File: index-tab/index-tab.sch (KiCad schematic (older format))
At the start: 18 parts, among them J1 USB_C_Receptacle_USB2.0, SW1 SW_Push, U1 ATmega32U2-AU, Y1 Crystal_GND24

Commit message: Updated somevalues, and fixed the pin layout
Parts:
- C4, C5: value C -> 22p
- F1: value Polyfuse -> 500mA
- R1, R2: value R -> 5.1K
- Y1: value Crystal_GND24 -> 16MHz
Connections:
- net labels added: COL10, COL11, COL12, COL6, COL7, COL8, COL9
- net labels removed: ROW10, ROW11, ROW12, ROW6, ROW7, ROW8, ROW9
- wire segments 110 -> 111
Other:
- moved on the sheet: R2
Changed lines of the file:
@@
 P 3700 2450
 F 0 "C4" V 3448 2450 50  0000 C CNN
-F 1 "C" V 3539 2450 50  0000 C CNN
+F 1 "22p" V 3539 2450 50  0000 C CNN
 F 2 "" H 3738 2300 50  0001 C CNN
 F 3 "~" H 3700 2450 50  0001 C CNN
@@
 P 3700 2850
 F 0 "C5" V 3448 2850 50  0000 C CNN
-F 1 "C" V 3539 2850 50  0000 C CNN
+F 1 "22p" V 3539 2850 50  0000 C CNN
 F 2 "" H 3738 2700 50  0001 C CNN
 F 3 "~" H 3700 2850 50  0001 C CNN
@@
 P 4100 2650
 F 0 "Y1" V 4146 2406 50  0000 R CNN
-F 1 "Crystal_GND24" V 4055 2406 50  0000 R CNN
+F 1 "16MHz" V 4055 2406 50  0000 R CNN
 F 2 "" H 4100 2650 50  0001 C CNN
 F 3 "~" H 4100 2650 50  0001 C CNN
@@
 L power:GND #PWR06
 U 1 1 5E49637F
-P 2600 2450
-F 0 "#PWR06" H 2600 2200 50  0001 C CNN
-F 1 "GND" H 2605 2277 50  0000 C CNN
-F 2 "" H 2600 2450 50  0001 C CNN
-F 3 "" H 2600 2450 50  0001 C CNN
-	1    2600 2450
+P 2650 2450
+F 0 "#PWR06" H 2650 2200 50  0001 C CNN
+F 1 "GND" H 2655 2277 50  0000 C CNN
+F 2 "" H 2650 2450 50  0001 C CNN
+F 3 "" H 2650 2450 50  0001 C CNN
+	1    2650 2450
 	-1   0    0    1
 $EndComp
@@
 L Device:R R2
 U 1 1 5E496DB2
-P 2700 2700
-F 0 "R2" H 2630 2654 50  0000 R CNN
-F 1 "R" H 2630 2745 50  0000 R CNN
-F 2 "" V 2630 2700 50  0001 C CNN
-F 3 "~" H 2700 2700 50  0001 C CNN
-	1    2700 2700
+P 2800 2700
+F 0 "R2" H 2730 2654 50  0000 R CNN
+F 1 "5.1K" H 2730 2745 50  0000 R CNN
+F 2 "" V 2730 2700 50  0001 C CNN
+F 3 "~" H 2800 2700 50  0001 C CNN
+	1    2800 2700
 	-1   0    0    1
 $EndComp
@@
 P 2450 2700
 F 0 "R1" H 2380 2654 50  0000 R CNN
-F 1 "R" H 2380 2745 50  0000 R CNN
+F 1 "5.1K" H 2380 2745 50  0000 R CNN
 F 2 "" V 2380 2700 50  0001 C CNN
 F 3 "~" H 2450 2700 50  0001 C CNN
@@
 $EndComp
 Wire Wire Line
-	2700 2550 2600 2550
-Wire Wire Line
-	2600 2550 2600 2450
-Wire Wire Line
-	2450 2550 2600 2550
-Connection ~ 2600 2550
-Wire Wire Line
 	2100 3100 2450 3100
 Wire Wire Line
 	2450 3100 2450 2850
 Wire Wire Line
-	2100 3200 2700 3200
-Wire Wire Line
-	2700 3200 2700 2850
+	2800 3200 2800 2850
 $Comp
 L power:+5V #PWR05
@@
 P 2250 2050
 F 0 "F1" H 2338 2096 50  0000 L CNN
-F 1 "Polyfuse" H 2338 2005 50  0000 L CNN
+F 1 "500mA" H 2338 2005 50  0000 L CNN
 F 2 "" H 2300 1850 50  0001 L CNN
 F 3 "~" H 2250 2050 50  0001 C CNN
@@
 	2850 3450 3000 3450
 Text GLabel 6700 3850 2    50   Input ~ 0
+COL6
+Text GLabel 6700 3950 2    50   Input ~ 0
+COL7
+Text GLabel 6700 4050 2    50   Input ~ 0
+COL8
+Text GLabel 6700 4150 2    50   Input ~ 0
+COL9
+Text GLabel 6700 4250 2    50   Input ~ 0
+COL10
+Text GLabel 6700 4350 2    50   Input ~ 0
+COL11
+Wire Wire Line
+	6500 3850 6700 3850
+Wire Wire Line
+	6500 3950 6700 3950
+Wire Wire Line
+	6500 4050 6700 4050
+Wire Wire Line
+	6500 4150 6700 4150
+Wire Wire Line
+	6500 4250 6700 4250
+Wire Wire Line
+	6500 4350 6700 4350
+Text GLabel 6700 2950 2    50   Input ~ 0
 COL0
-Text GLabel 6700 3950 2    50   Input ~ 0
+Text GLabel 6700 3050 2    50   Input ~ 0
 COL1
-Text GLabel 6700 4050 2    50   Input ~ 0
+Text GLabel 6700 3250 2    50   Input ~ 0
 COL2
-Text GLabel 6700 4150 2    50   Input ~ 0
+Text GLabel 6700 3350 2    50   Input ~ 0
 COL3
-Text GLabel 6700 4250 2    50   Input ~ 0
+Text GLabel 6700 3450 2    50   Input ~ 0
 COL4
-Text GLabel 6700 4350 2    50   Input ~ 0
+Text GLabel 6700 3550 2    50   Input ~ 0
 COL5
-Wire Wire Line
-	6500 3850 6700 3850
-Wire Wire Line
-	6500 3950 6700 3950
-Wire Wire Line
-	6500 4050 6700 4050
-Wire Wire Line
-	6500 4150 6700 4150
-Wire Wire Line
-	6500 4250 6700 4250
-Wire Wire Line
-	6500 4350 6700 4350
-Text GLabel 6700 2350 2    50   Input ~ 0
-ROW0
-Text GLabel 6700 2450 2    50   Input ~ 0
-ROW1
-Text GLabel 6700 2550 2    50   Input ~ 0
-ROW2
-Text GLabel 6700 2650 2    50   Input ~ 0
-ROW3
-Text GLabel 6700 2750 2    50   Input ~ 0
-ROW4
-Text GLabel 6700 2850 2    50   Input ~ 0
-ROW5
-Text GLabel 6700 2950 2    50   Input ~ 0
-ROW6
-Text GLabel 6700 3050 2    50   Input ~ 0
-ROW7
-Text GLabel 6700 3250 2    50   Input ~ 0
-ROW8
-Text GLabel 6700 3350 2    50   Input ~ 0
-ROW9
-Text GLabel 6700 3450 2    50   Input ~ 0
-ROW10
-Text GLabel 6700 3550 2    50   Input ~ 0
-ROW11
 Text GLabel 6700 4450 2    50   Input ~ 0
-ROW12
+COL12
 Wire Wire Line
 	6500 2350 6700 2350
@@
 F1 "matrix.sch" 50
 $EndSheet
+Wire Wire Line
+	2100 3200 2800 3200
+Wire Wire Line
+	2650 2450 2800 2450
+Wire Wire Line
+	2800 2450 2800 2550
+Wire Wire Line
+	2450 2550 2450 2450
+Wire Wire Line
+	2450 2450 2650 2450
+Connection ~ 2650 2450
+Text GLabel 6700 2850 2    50   Input ~ 0
+ROW5
+Text GLabel 6700 2750 2    50   Input ~ 0
+ROW4
+Text GLabel 6700 2650 2    50   Input ~ 0
+ROW3
+Text GLabel 6700 2550 2    50   Input ~ 0
+ROW2
+Text GLabel 6700 2450 2    50   Input ~ 0
+ROW1
+Text GLabel 6700 2350 2    50   Input ~ 0
+ROW0
 $EndSCHEMATC

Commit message: Change to u4, added files for backlight and rgb
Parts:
- removed U1: ATmega32U2-AU, Package_QFP:TQFP-32_7x7mm_P0.8mm, symbol MCU_Microchip_ATmega:ATmega32U2-AU
- added LS1: Speaker, symbol Device:Speaker
- added R7: 1K, symbol Device:R
- added U1: ATmega32U4-MU, Package_DFN_QFN:QFN-44-1EP_7x7mm_P0.5mm_EP5.2x5.2mm, symbol MCU_Microchip_ATmega:ATmega32U4-MU
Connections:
- net labels added: BACKLIGHT, RGB
- wire segments 111 -> 120
- no-connect marks 2 -> 7
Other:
- moved on the sheet: C4, C5, C6, R5, R6, SW1, Y1

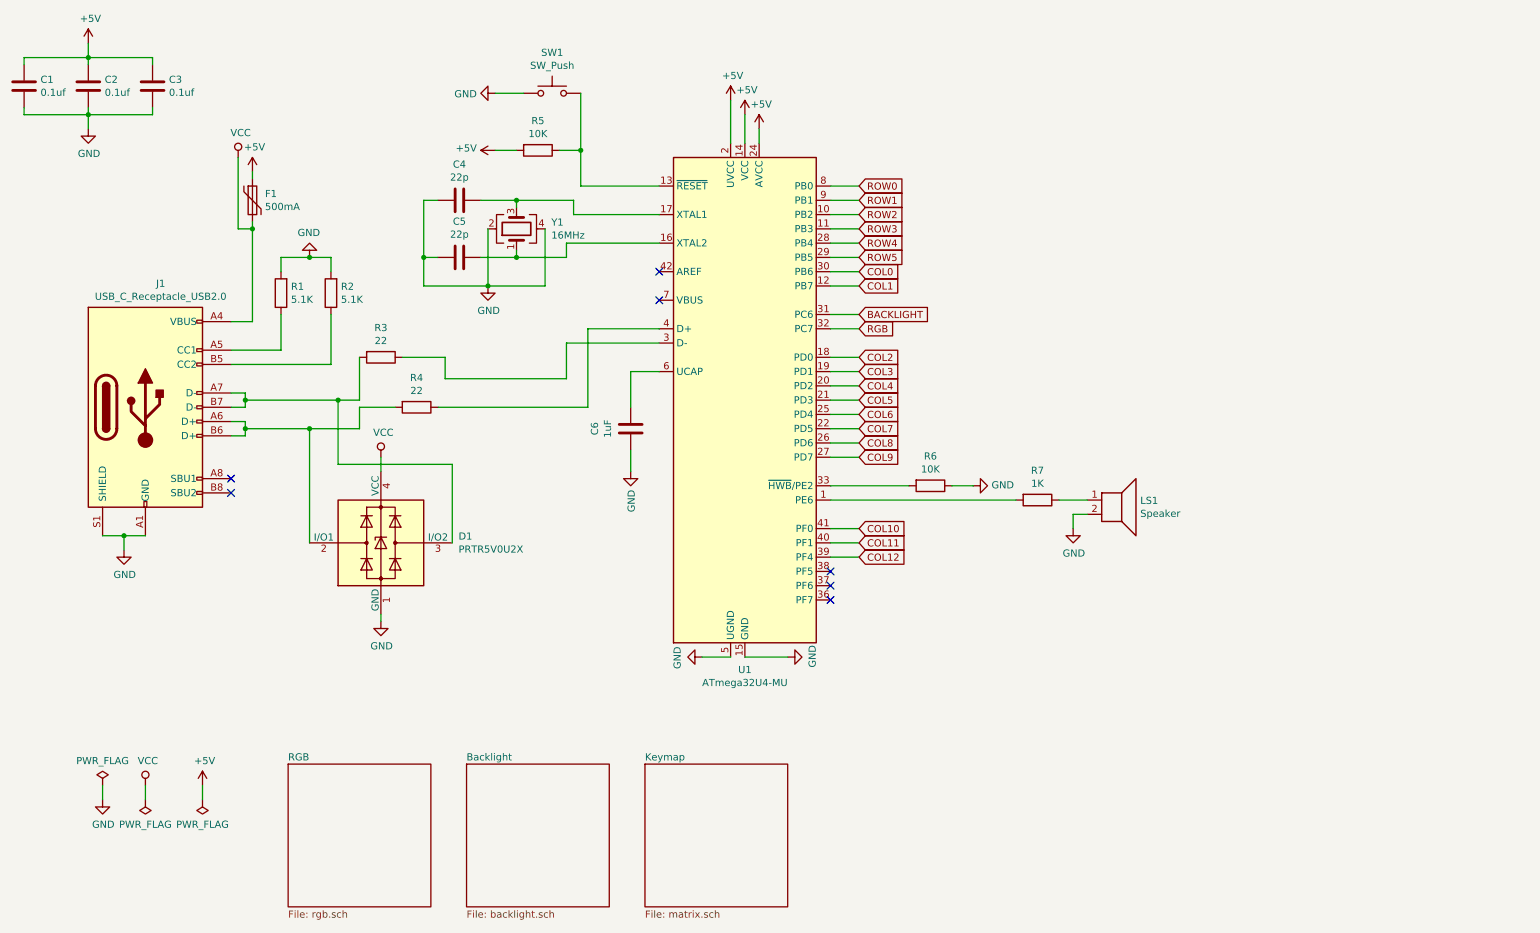
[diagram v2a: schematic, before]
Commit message: changed some labels, and hopefully done with the atmega32u4 changes
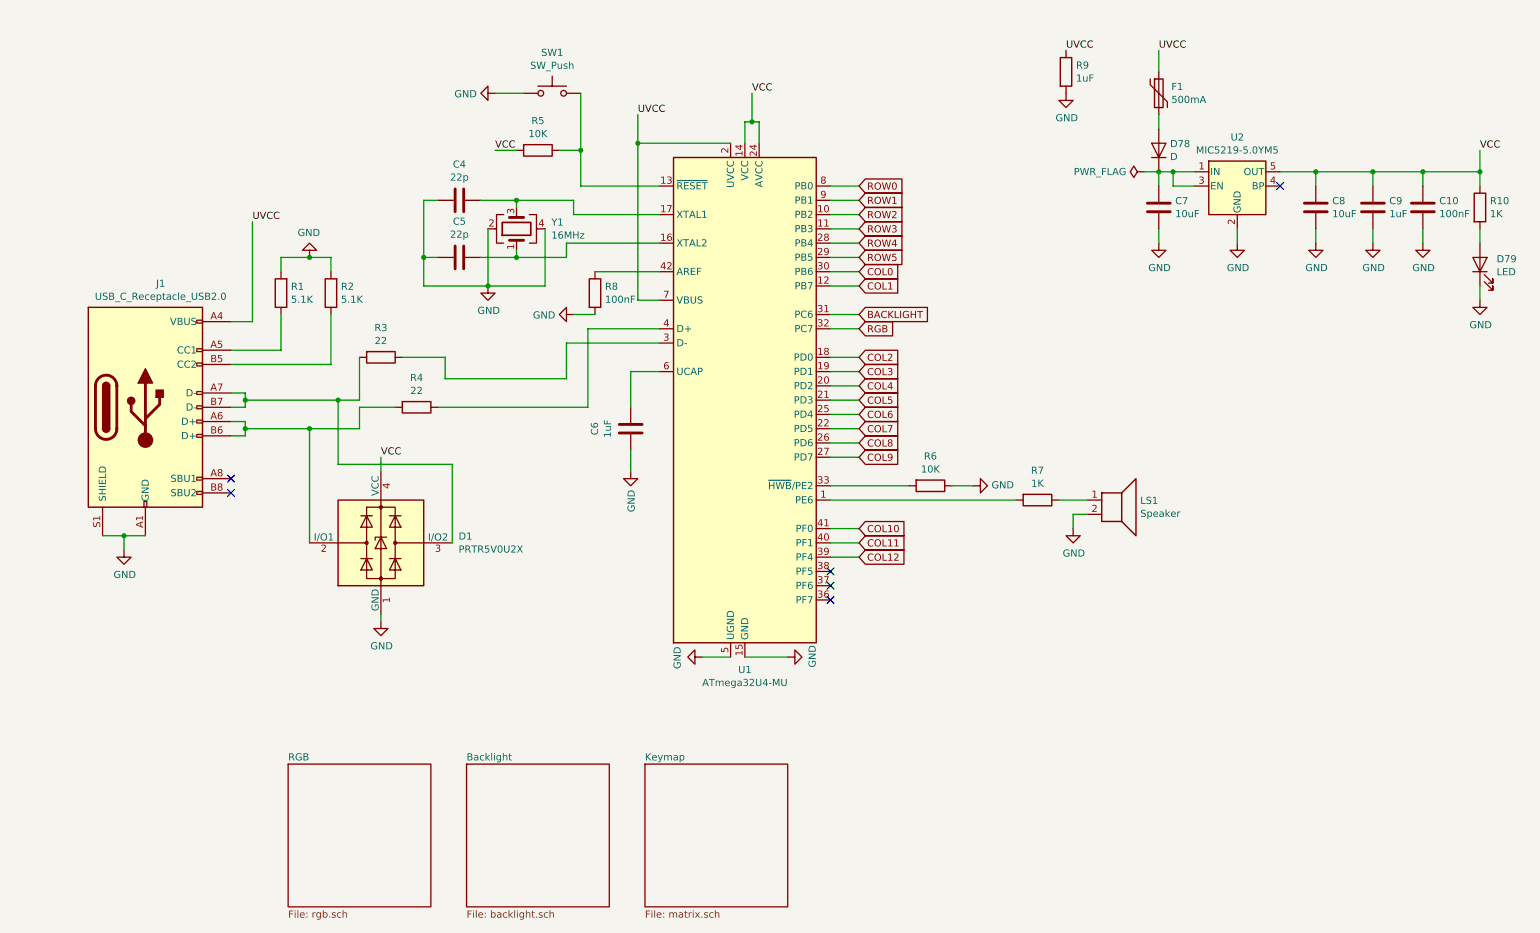
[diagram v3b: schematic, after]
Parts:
- removed C1, C2, C3: 0.1uf, symbol Device:C
- added C10: 100nF, symbol Device:C
- added C7, C8: 10uF, symbol Device:C
- added C9: 1uF, symbol Device:C
- added D78: D, symbol Device:D
- added D79: LED, symbol Device:LED
- added R10: 1K, symbol Device:R
- added R8: 100nF, symbol Device:R
- added R9: 1uF, symbol Device:R
- added U2: MIC5219-5.0YM5, Package_TO_SOT_SMD:SOT-23-5, symbol Regulator_Linear:MIC5219-5.0YM5
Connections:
- net GND: now also C10.2, C7.2, C8.2, C9.2, D79.1 (K), R8.2, R9.2, U2.2 (GND)
- net VCC: now also R5.2, U1.14 (VCC), U1.24 (AVCC), U1.34 (VCC), U1.44 (AVCC), C10.1, C8.1, C9.1, R10.1, U2.5 (OUT); no longer F1.2, J1.A4 (VBUS), J1.A9 (VBUS), J1.B4 (VBUS), J1.B9 (VBUS)
- net at U1.42 (AREF): now also R8.1
- net UVCC: now reaches U1.7 (VBUS)
- net UVCC: now also F1.1, J1.A4 (VBUS), J1.A9 (VBUS), J1.B4 (VBUS), J1.B9 (VBUS), U1.2 (UVCC), R9.1
- removed net +5V: F1.1, R5.2, U1.14 (VCC), U1.2 (UVCC), U1.24 (AVCC), U1.34 (VCC), U1.44 (AVCC)
- new net: D79.2 (A), R10.2
- new net: C7.1, D78.1 (K), U2.1 (IN), U2.3 (EN)
- new net: D78.2 (A), F1.2
- no-connect marks 7 -> 6
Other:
- moved on the sheet: F1

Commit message: Added footprints to all components, and done some formatting
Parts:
- removed R8: 100nF, symbol Device:R
- removed R9: 1uF, symbol Device:R
- added C1: 100nF, Capacitor_SMD:C_0603_1608Metric_Pad1.05x0.95mm_HandSolder, symbol Device:C
- added C2: 1uF, Capacitor_SMD:C_0603_1608Metric_Pad1.05x0.95mm_HandSolder, symbol Device:C
- C10, C4, C5, C6, C7, C8, C9: footprint (none) -> Capacitor_SMD:C_0603_1608Metric_Pad1.05x0.95mm_HandSolder
- D78: footprint (none) -> Diode_SMD:D_SOD-123
- D79: footprint (none) -> LED_THT:LED_D3.0mm_FlatTop
- F1: footprint (none) -> Fuse:Fuse_0805_2012Metric_Pad1.15x1.40mm_HandSolder
- J1: footprint (none) -> Connector_USB:USB_C_Receptacle_HRO_TYPE-C-31-M-12
- LS1: footprint (none) -> Buzzer_Beeper:Buzzer_12x9.5RM7.6
- R1, R10, R2, R3, R4, R5, R6, R7: footprint (none) -> Resistor_SMD:R_0201_0603Metric
- SW1: footprint (none) -> Button_Switch_SMD:SW_SPST_CK_RS282G05A3
- Y1: footprint (none) -> Crystal:Crystal_SMD_3225-4Pin_3.2x2.5mm_HandSoldering
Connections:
- net GND: now also C5.1, C1.1, C2.2; no longer C5.2
- net UVCC: now also C2.1
- net XTAL1: now reaches U1.17 (XTAL1), Y1.3
- net XTAL1: now also C5.2; no longer C4.1
- net XTAL2: now reaches U1.16 (XTAL2), Y1.1
- net XTAL2: now also C4.1; no longer C5.1
- net at U1.42 (AREF): now also C1.2
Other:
- moved on the sheet: C4, C5, D1, R1, R2, R3, R4, Y1

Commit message: Working PCB, plus images
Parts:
- removed LS1: Speaker, Buzzer_Beeper:Buzzer_12x9.5RM7.6, symbol Device:Speaker
- removed R7: 1K, Resistor_SMD:R_0201_0603Metric, symbol Device:R
- C1: renamed from C4; footprint Capacitor_SMD:C_0603_1608Metric_Pad1.05x0.95mm_HandSolder -> Capacitor_SMD:C_1206_3216Metric_Pad1.42x1.75mm_HandSolder
- C2: renamed from C5; footprint Capacitor_SMD:C_0603_1608Metric_Pad1.05x0.95mm_HandSolder -> Capacitor_SMD:C_1206_3216Metric_Pad1.42x1.75mm_HandSolder
- C3: renamed from C1; footprint Capacitor_SMD:C_0603_1608Metric_Pad1.05x0.95mm_HandSolder -> Capacitor_SMD:C_1206_3216Metric_Pad1.42x1.75mm_HandSolder
- C4: renamed from C6; footprint Capacitor_SMD:C_0603_1608Metric_Pad1.05x0.95mm_HandSolder -> Capacitor_SMD:C_1206_3216Metric_Pad1.42x1.75mm_HandSolder
- C5: renamed from C2; footprint Capacitor_SMD:C_0603_1608Metric_Pad1.05x0.95mm_HandSolder -> Capacitor_SMD:C_1206_3216Metric_Pad1.42x1.75mm_HandSolder
- C6: renamed from C7; footprint Capacitor_SMD:C_0603_1608Metric_Pad1.05x0.95mm_HandSolder -> Capacitor_SMD:C_1206_3216Metric_Pad1.42x1.75mm_HandSolder
- C7: renamed from C8; footprint Capacitor_SMD:C_0603_1608Metric_Pad1.05x0.95mm_HandSolder -> Capacitor_SMD:C_1206_3216Metric_Pad1.42x1.75mm_HandSolder
- C8: renamed from C9; footprint Capacitor_SMD:C_0603_1608Metric_Pad1.05x0.95mm_HandSolder -> Capacitor_SMD:C_1206_3216Metric_Pad1.42x1.75mm_HandSolder
- C9: renamed from C10; footprint Capacitor_SMD:C_0603_1608Metric_Pad1.05x0.95mm_HandSolder -> Capacitor_SMD:C_1206_3216Metric_Pad1.42x1.75mm_HandSolder
- D102: renamed from D78; footprint Diode_SMD:D_SOD-123 -> Diode_SMD:D_1206_3216Metric_Pad1.42x1.75mm_HandSolder
- D103: renamed from D79; footprint LED_THT:LED_D3.0mm_FlatTop -> LED_SMD:LED_1206_3216Metric_Pad1.42x1.75mm_HandSolder
- R1, R2, R3, R4, R5, R6: footprint Resistor_SMD:R_0201_0603Metric -> Resistor_SMD:R_1206_3216Metric_Pad1.42x1.75mm_HandSolder
- R7: renamed from R10; footprint Resistor_SMD:R_0201_0603Metric -> Resistor_SMD:R_1206_3216Metric_Pad1.42x1.75mm_HandSolder
- U2: footprint Package_TO_SOT_SMD:SOT-23-5 -> Package_TO_SOT_SMD:SOT-23-5_HandSoldering
- renumbered D1 to D101
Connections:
- net BACKLIGHT is gone; now on net ROW1: U1.31 (PC6)
- net RGB is gone; now on net ROW0: U1.32 (PC7)
- net COL0: now also U1.22 (PD5); no longer U1.30 (PB6)
- net COL1: now also U1.21 (PD3); no longer U1.12 (PB7)
- net COL2: now also U1.20 (PD2); no longer U1.18 (PD0)
- net COL4: now also U1.18 (PD0); no longer U1.20 (PD2)
- net COL5: now also U1.12 (PB7); no longer U1.21 (PD3)
- net COL6: now also U1.11 (PB3); no longer U1.25 (PD4)
- net COL7: now also U1.10 (PB2); no longer U1.22 (PD5)
- net COL8: now also U1.9 (PB1); no longer U1.26 (PD6)
- net COL9: now also U1.8 (PB0); no longer U1.27 (PD7)
- net ROW0: no longer U1.8 (PB0)
- net ROW1: no longer U1.9 (PB1)
- net ROW2: now also U1.30 (PB6); no longer U1.10 (PB2)
- net ROW3: now also U1.29 (PB5); no longer U1.11 (PB3)
- net ROW5: now also U1.27 (PD7); no longer U1.29 (PB5)
- no-connect marks 6 -> 9
